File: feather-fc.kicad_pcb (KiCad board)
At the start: 2 copper layers, 50.8 x 22.9 mm, 23 parts, among them M1 Motor_Servo, M2 Motor_Servo, M3 Motor_Servo, M4 Motor_Servo, M5 Motor_Servo, M6 Motor_Servo, M7 Motor_Servo, M8 Motor_Servo, SW1 Mode_SW, SW3 Bind_SW, U3 MCP1700-3302E/TO

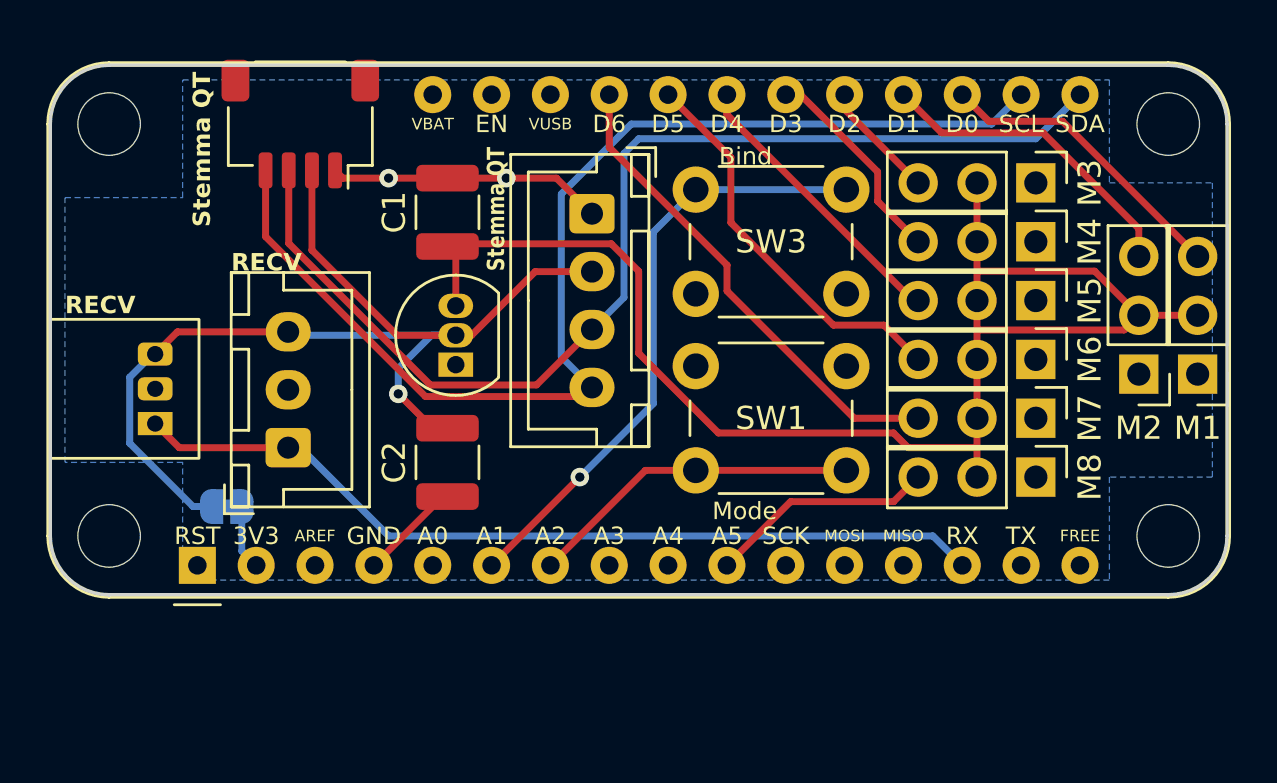
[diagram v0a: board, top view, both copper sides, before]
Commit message: Version 2: Fix the voltage regulator wiring
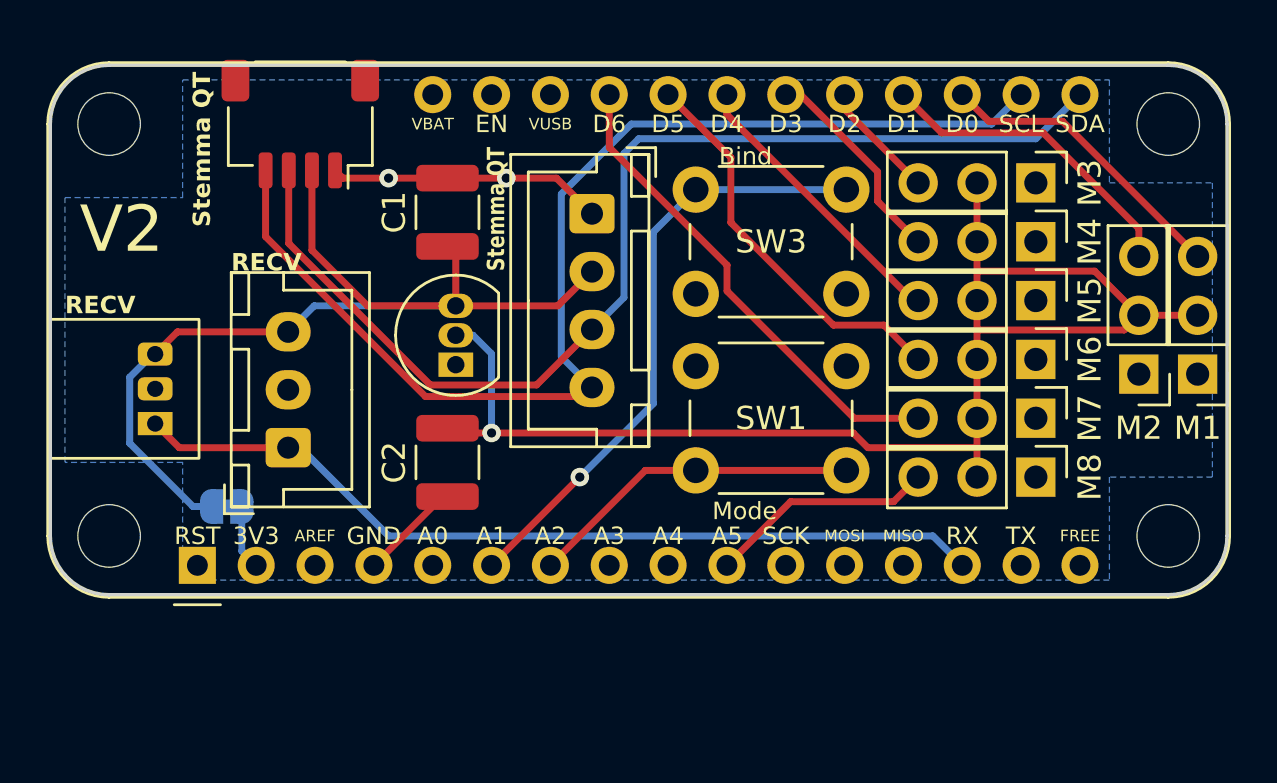
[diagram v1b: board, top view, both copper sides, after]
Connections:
- C1 pad 1: BEC_POWER -> +3.3V
- C2 pad 1: +3.3V -> BEC_POWER
- U3 pad 2: +3.3V -> BEC_POWER
- U3 pad 3: BEC_POWER -> +3.3V
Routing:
- net +3.3V: track 47.5 -> 42.7 mm, vias 1 -> 0
- net BEC_POWER: track 61.4 -> 58.8 mm, vias 0 -> 1
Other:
- board text added: "JLCJLCJLCJLC"
- board text added: "V2"

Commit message: Version 3 layout 2
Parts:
- removed M8: Motor_Servo, Connector_PinHeader_2.54mm:PinHeader_1x03_P2.54mm_Vertical
- removed U5: ~, Connector_JST:JST_XH_B3B-XH-A_1x03_P2.50mm_Vertical
- added D1: S2M-TP, Diode_SMD:D_SMB, F.Cu at (44.2, 42.4)
- added JP2: SolderJumper_2_Open, Jumper:SolderJumper-2_P1.3mm_Open_RoundedPad1.0x1.5mm, B.Cu at (44.2, 42.4)
- added SW2: Bind_SW, Button_Switch_THT:SW_PUSH_6mm, F.Cu at (64.0, 35.3)
- SW3: value Bind_SW -> Reset_SW
- U4: value ~ -> MCP1703Ax-300xxTT; footprint Connector_JST:JST_XH_B4B-XH-A_1x04_P2.50mm_Vertical -> Package_TO_SOT_SMD:SOT-23
- moved U2 41.8 mm to (71.7, 39.1), turned to -90 degrees
- moved M1 41.4 mm to (33.7, 41.9), turned to 90 degrees
- moved M2 38.7 mm to (33.7, 39.4), turned to 90 degrees
- moved U1 37.4 mm to (73.2, 33.7), turned to 90 degrees
- moved M7 37.0 mm to (33.7, 26.7), turned to 90 degrees
- moved M6 35.4 mm to (33.7, 29.2), turned to 90 degrees
- moved M3 34.9 mm to (33.7, 36.8), turned to 90 degrees
- moved M5 34.5 mm to (33.7, 31.8), turned to 90 degrees
- moved M4 34.3 mm to (33.7, 34.3), turned to 90 degrees
- moved U4 22.8 mm to (57.8, 52.7)
- moved JP1 14.8 mm to (46.0, 37.3), turned to -90 degrees
- moved SW3 12.6 mm to (49.9, 42.9), turned to 90 degrees
- moved C1 7.31 mm to (49.8, 32.8), turned to 0 degrees
- moved C2 4.50 mm to (44.2, 38.4), turned to 180 degrees
- moved SW1 4.19 mm to (64.0, 42.9)
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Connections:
- A1 pad 1: unconnected-(A1-~{RESET}-Pad1) -> Net-(A1-~{RESET})
- A1 pad 10: /PWM8 -> unconnected-(A1-A5-Pad10)
- A1 pad 2: Net-(A1-3V3) -> +3.3V
- C1 pad 1: +3.3V -> Net-(JP1-A)
- JP1 pad 1: Net-(A1-3V3) -> Net-(JP1-A)
- M1 pad 2: BEC_POWER -> Net-(D1-A)
- M2 pad 2: BEC_POWER -> Net-(D1-A)
- M3 pad 2: BEC_POWER -> Net-(D1-A)
- M4 pad 2: BEC_POWER -> Net-(D1-A)
- M5 pad 2: BEC_POWER -> Net-(D1-A)
- M6 pad 2: BEC_POWER -> Net-(D1-A)
- M7 pad 2: BEC_POWER -> Net-(D1-A)
- SW3 pad 1: Net-(A1-A1) -> Net-(A1-~{RESET})
- U3 pad 3: +3.3V -> Net-(JP1-A)
- U4 pad 1: GND -> unconnected-(U4-GND-Pad1)
- U4 pad 2: +3.3V -> unconnected-(U4-VO-Pad2)
- U4 pad 3: /SDA -> unconnected-(U4-VI-Pad3)
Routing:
- net BEC_POWER: track 58.8 -> 10.6 mm
- net /SCL: track 50.5 -> 7.08 mm
- net /SDA: track 48.7 -> 8.35 mm
- net Net-(A1-~{RESET}): track 0.00 -> 26.3 mm, vias 0 -> 1
- net Net-(D1-A): track 0.00 -> 26.3 mm, vias 0 -> 1
- net Net-(A1-RX): track 37.9 -> 11.6 mm
- net /PWM1: track 13.1 -> 37.1 mm
- net /PMW3: track 5.13 -> 27.7 mm
- net /PWM2: track 13.8 -> 32.4 mm
- net /PWM4: track 9.09 -> 23.1 mm
- net +3.3V: track 42.7 -> 55.9 mm, vias 0 -> 2
- net GND: track 16.2 -> 6.27 mm
- net /PWM8: track 9.83 -> 0.00 mm
- net /PWM7: track 21.1 -> 12.0 mm
- net /PWM5: track 12.4 -> 18.4 mm
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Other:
- board text added: "+"
- board text added: "-"
- board text added: "Capacitor bypass"
- board text added: "PWM"
- board text added: "Regulator output"
- board text added: "Reset"
- board text added: "V3"
- board text removed: "3v to feather"
- board text removed: "V2"

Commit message: Verion 3 final revision
General cleanup and rearrangement
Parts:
- removed the REF** at (73.7, 27.9)
- removed U4: MCP1703Ax-300xxTT, Package_TO_SOT_SMD:SOT-23
- moved U1 2.52 mm to (73.3, 31.1)
- moved U2 1.28 mm to (71.5, 37.9)
- moved C1 0.54 mm to (49.8, 33.3)
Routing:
- net Net-(A1-A1): track 21.7 -> 28.2 mm
- net /SDA: track 8.35 -> 5.97 mm
- net +3.3V: track 55.9 -> 57.8 mm
- net /SCL: track 7.08 -> 5.25 mm
- net GND: track 6.27 -> 4.51 mm, vias 2 -> 3
- net Net-(D1-A): track 26.3 -> 25.8 mm
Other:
- board text added: "Diode bypass"
- board text added: "~"
- board text removed: "Capacitor bypass"
- board text removed: "PWM"
